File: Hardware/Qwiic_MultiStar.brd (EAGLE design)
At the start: 62.5 x 59.5 mm, 23 parts, among them J1 QWIIC_RIGHT_ANGLE, J2 QWIIC_RIGHT_ANGLE, J3 QWIIC_RIGHT_ANGLE, J4 QWIIC_RIGHT_ANGLE, J5 QWIIC_RIGHT_ANGLE

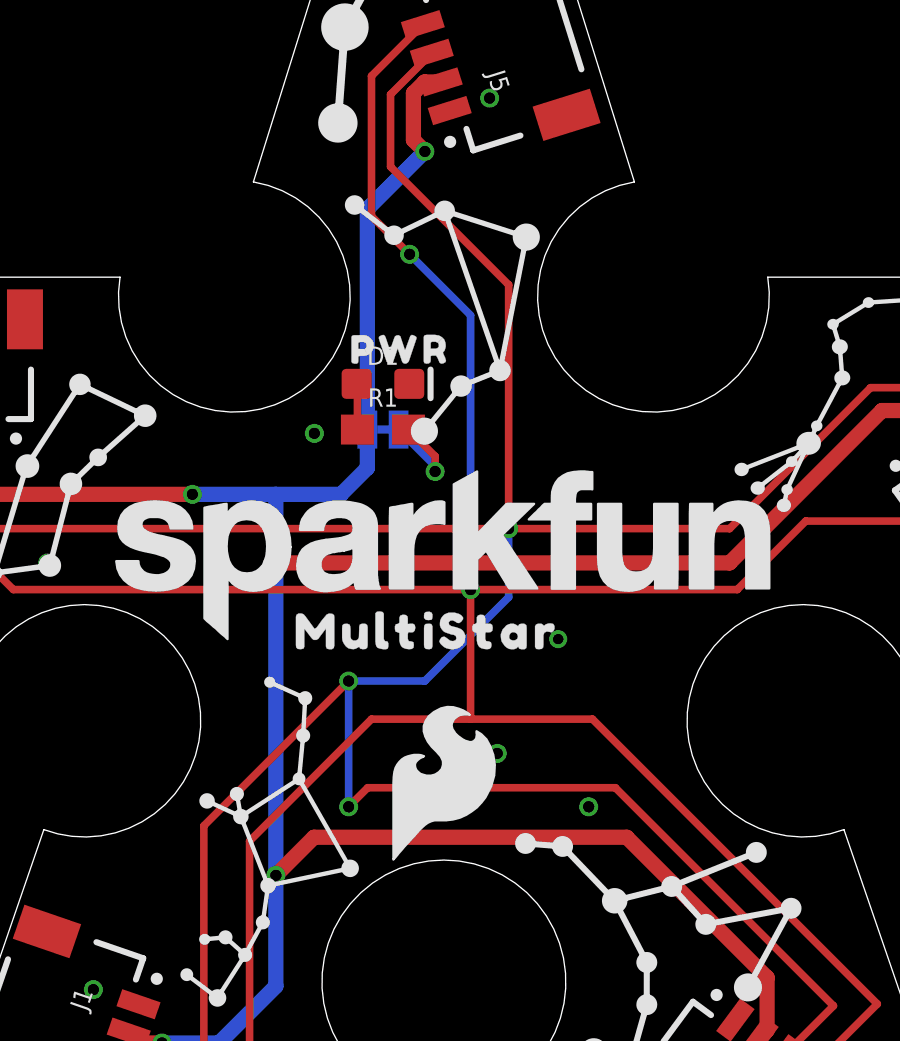
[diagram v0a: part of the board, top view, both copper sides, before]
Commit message: Slight silk nudge
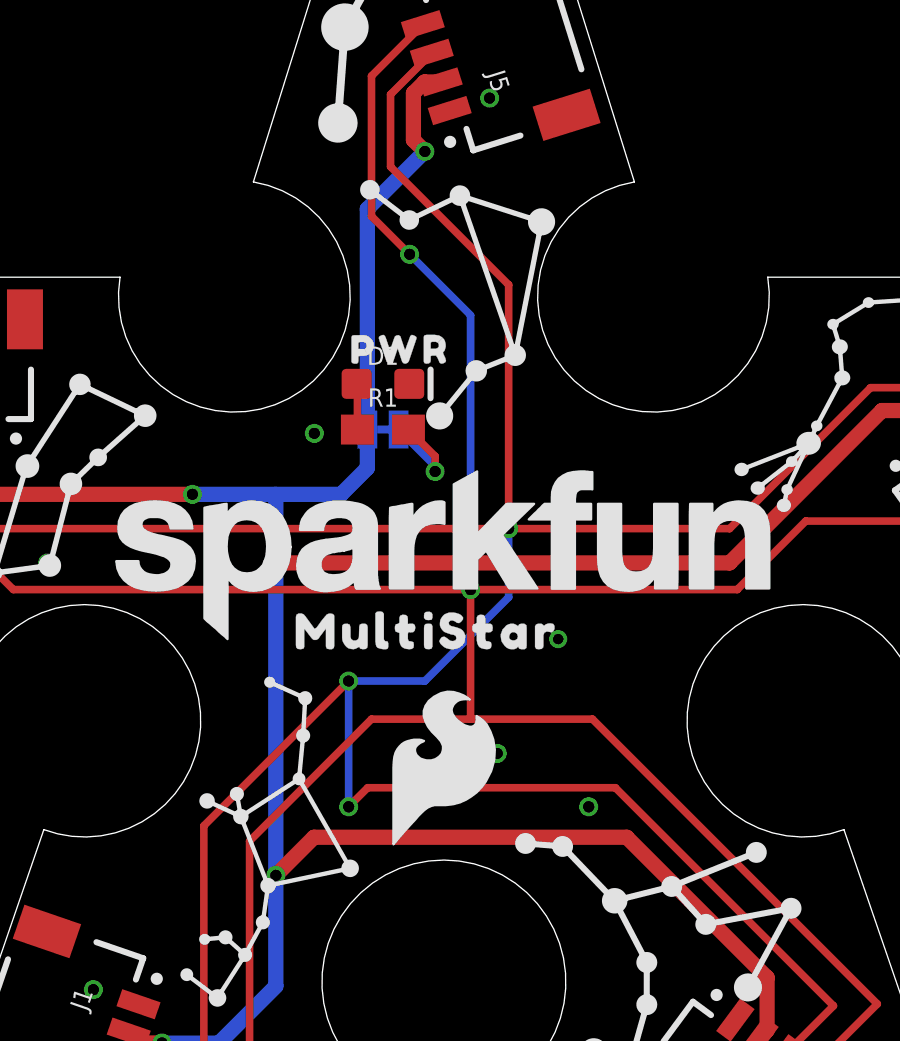
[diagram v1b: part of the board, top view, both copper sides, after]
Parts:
- moved U$2 0.51 mm to (31.8, 22.4)

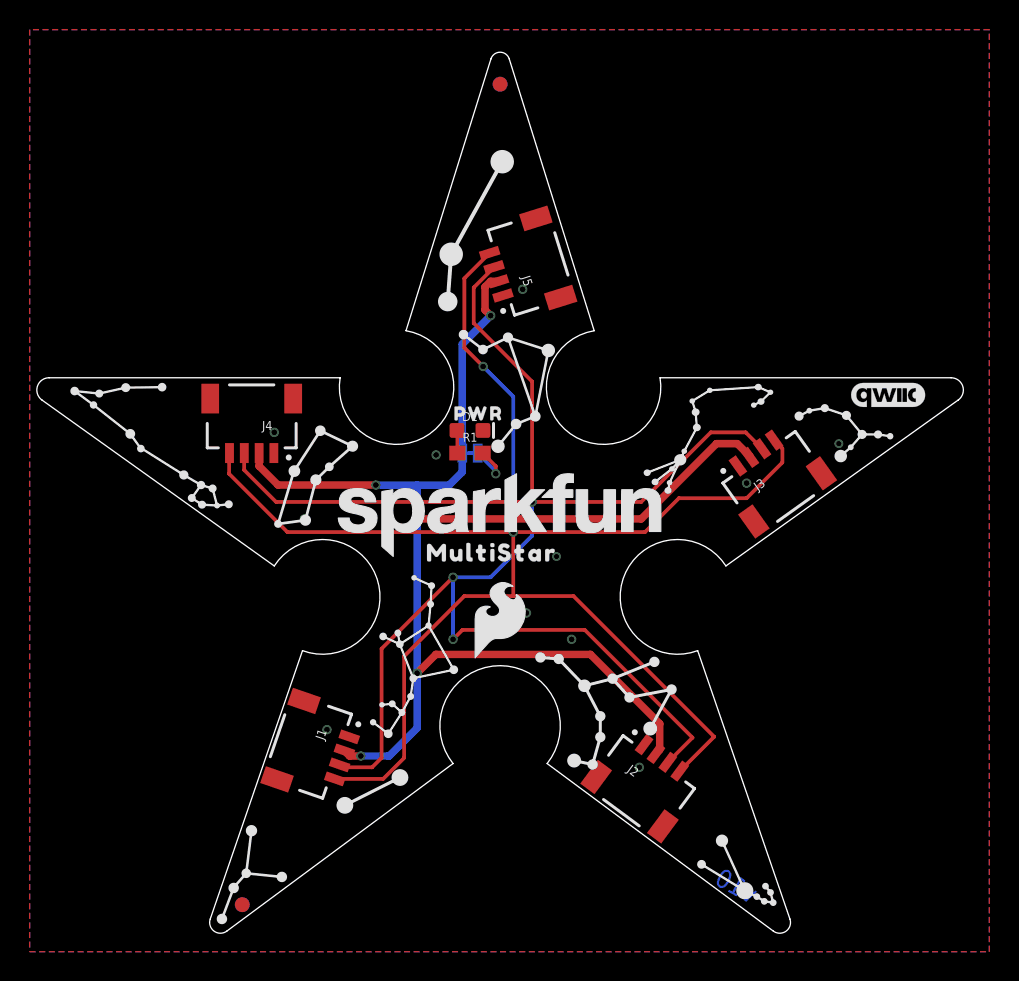
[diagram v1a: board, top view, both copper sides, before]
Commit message: Small update
-Moved some silk to not be obstructed
-Moved vias to not obstruct silk
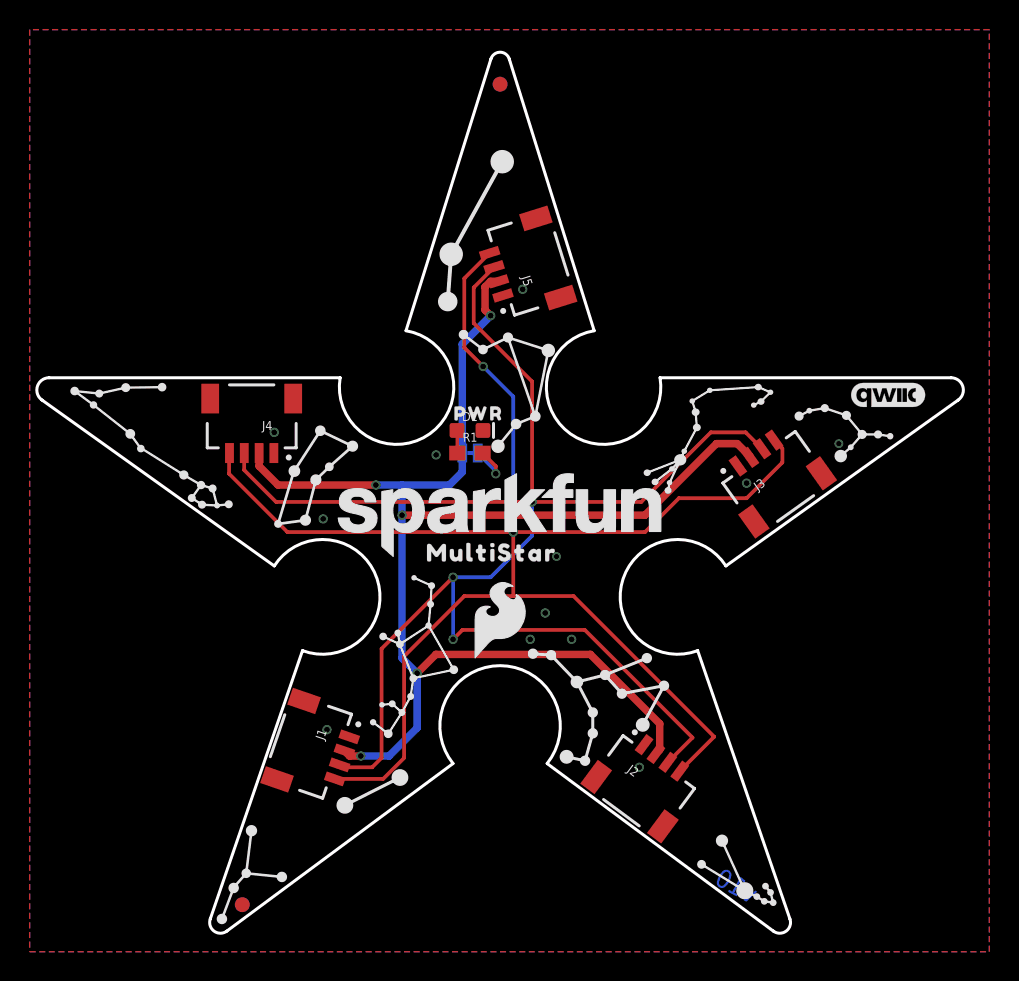
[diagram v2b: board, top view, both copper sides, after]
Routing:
- net 3.3V: track 98.2 -> 99.5 mm
